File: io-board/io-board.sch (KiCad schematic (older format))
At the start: 12 parts, among them J1 Expansion, J2 Expansion, J3 Conn_01x12, J4 Conn_01x12, J5 Conn_01x06, U1 W65C22NxP, U2 W65C51NxP, U3 74HC138, X1 1.8432MHz

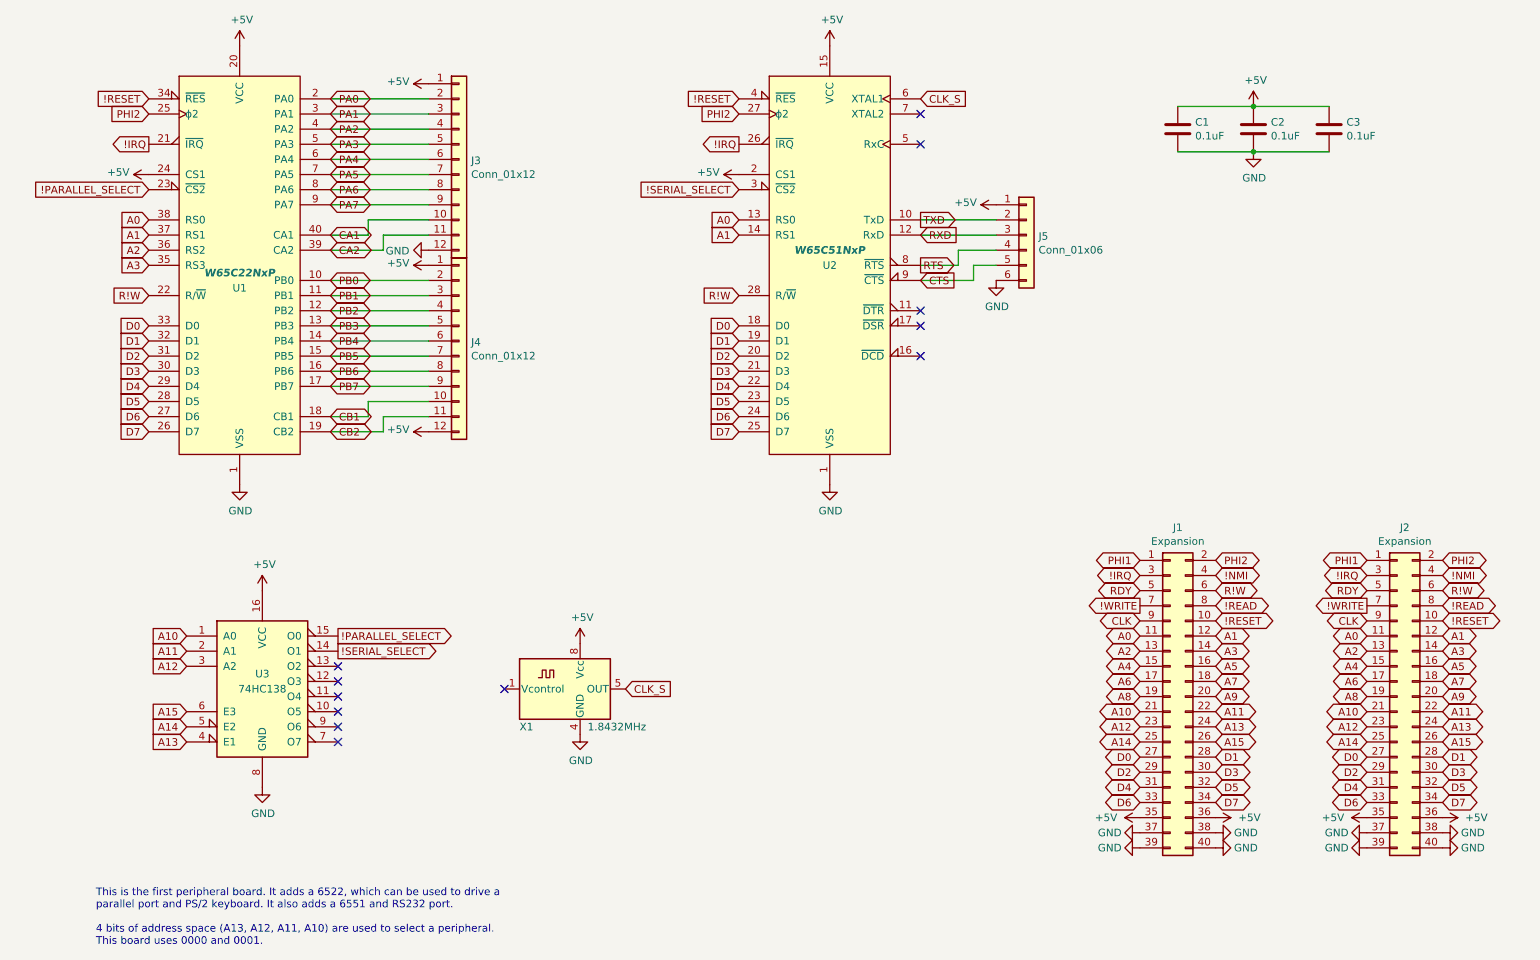
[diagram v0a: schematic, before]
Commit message: remove vga board, finish other boards
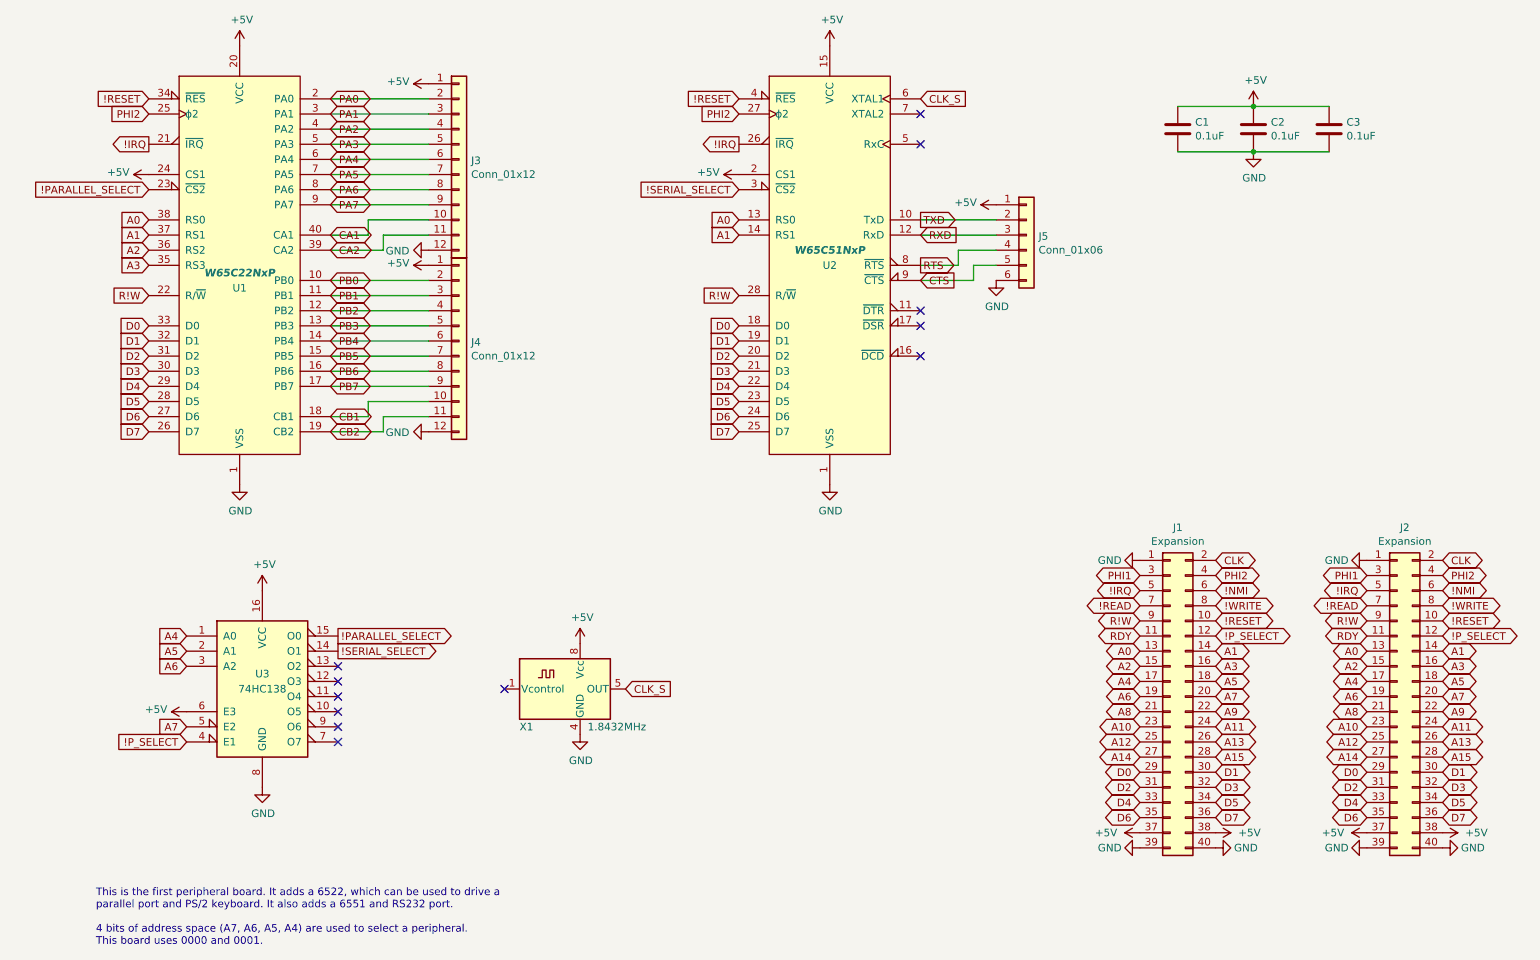
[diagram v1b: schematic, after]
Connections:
- net !IRQ: now also J1.5 (Pin_5), J2.5 (Pin_5); no longer J1.3 (Pin_3), J2.3 (Pin_3)
- net !NMI: now also J1.6 (Pin_6), J2.6 (Pin_6); no longer J1.4 (Pin_4), J2.4 (Pin_4)
- net !READ: now also J1.7 (Pin_7), J2.7 (Pin_7); no longer J1.8 (Pin_8), J2.8 (Pin_8)
- net !WRITE: now also J1.8 (Pin_8), J2.8 (Pin_8); no longer J1.7 (Pin_7), J2.7 (Pin_7)
- net +5V: now also J1.37 (Pin_37), J1.38 (Pin_38), J2.37 (Pin_37), J2.38 (Pin_38), U3.6 (E3); no longer J1.35 (Pin_35), J1.36 (Pin_36), J2.35 (Pin_35), J2.36 (Pin_36), J4.12 (Pin_12)
- net A0: now also J1.13 (Pin_13), J2.13 (Pin_13); no longer J1.11 (Pin_11), J2.11 (Pin_11)
- net A1: now also J1.14 (Pin_14), J2.14 (Pin_14); no longer J1.12 (Pin_12), J2.12 (Pin_12)
- net A10: now also J1.23 (Pin_23), J2.23 (Pin_23); no longer J1.21 (Pin_21), J2.21 (Pin_21), U3.1 (A0)
- net A11: now also J1.24 (Pin_24), J2.24 (Pin_24); no longer J1.22 (Pin_22), J2.22 (Pin_22), U3.2 (A1)
- net A12: now also J1.25 (Pin_25), J2.25 (Pin_25); no longer J1.23 (Pin_23), J2.23 (Pin_23), U3.3 (A2)
- net A13: now also J1.26 (Pin_26), J2.26 (Pin_26); no longer J1.24 (Pin_24), J2.24 (Pin_24), U3.4 (E1)
- net A14: now also J1.27 (Pin_27), J2.27 (Pin_27); no longer J1.25 (Pin_25), J2.25 (Pin_25), U3.5 (E2)
- net A15: now also J1.28 (Pin_28), J2.28 (Pin_28); no longer J1.26 (Pin_26), J2.26 (Pin_26), U3.6 (E3)
- net A2: now also J1.15 (Pin_15), J2.15 (Pin_15); no longer J1.13 (Pin_13), J2.13 (Pin_13)
- net A3: now also J1.16 (Pin_16), J2.16 (Pin_16); no longer J1.14 (Pin_14), J2.14 (Pin_14)
- net A4: now also J1.17 (Pin_17), J2.17 (Pin_17), U3.1 (A0); no longer J1.15 (Pin_15), J2.15 (Pin_15)
- net A5: now also J1.18 (Pin_18), J2.18 (Pin_18), U3.2 (A1); no longer J1.16 (Pin_16), J2.16 (Pin_16)
- net A6: now also J1.19 (Pin_19), J2.19 (Pin_19), U3.3 (A2); no longer J1.17 (Pin_17), J2.17 (Pin_17)
- net A7: now also J1.20 (Pin_20), J2.20 (Pin_20), U3.5 (E2); no longer J1.18 (Pin_18), J2.18 (Pin_18)
- net A8: now also J1.21 (Pin_21), J2.21 (Pin_21); no longer J1.19 (Pin_19), J2.19 (Pin_19)
- net A9: now also J1.22 (Pin_22), J2.22 (Pin_22); no longer J1.20 (Pin_20), J2.20 (Pin_20)
- net CLK: now also J1.2 (Pin_2), J2.2 (Pin_2); no longer J1.9 (Pin_9), J2.9 (Pin_9)
- net D0: now also J1.29 (Pin_29), J2.29 (Pin_29); no longer J1.27 (Pin_27), J2.27 (Pin_27)
- net D1: now also J1.30 (Pin_30), J2.30 (Pin_30); no longer J1.28 (Pin_28), J2.28 (Pin_28)
- net D2: now also J1.31 (Pin_31), J2.31 (Pin_31); no longer J1.29 (Pin_29), J2.29 (Pin_29)
- net D3: now also J1.32 (Pin_32), J2.32 (Pin_32); no longer J1.30 (Pin_30), J2.30 (Pin_30)
- net D4: now also J1.33 (Pin_33), J2.33 (Pin_33); no longer J1.31 (Pin_31), J2.31 (Pin_31)
- net D5: now also J1.34 (Pin_34), J2.34 (Pin_34); no longer J1.32 (Pin_32), J2.32 (Pin_32)
- net D6: now also J1.35 (Pin_35), J2.35 (Pin_35); no longer J1.33 (Pin_33), J2.33 (Pin_33)
- net D7: now also J1.36 (Pin_36), J2.36 (Pin_36); no longer J1.34 (Pin_34), J2.34 (Pin_34)
- net GND: now also J1.1 (Pin_1), J2.1 (Pin_1), J4.12 (Pin_12); no longer J1.37 (Pin_37), J1.38 (Pin_38), J2.37 (Pin_37), J2.38 (Pin_38)
- net PHI1: now also J1.3 (Pin_3), J2.3 (Pin_3); no longer J1.1 (Pin_1), J2.1 (Pin_1)
- net PHI2: now also J1.4 (Pin_4), J2.4 (Pin_4); no longer J1.2 (Pin_2), J2.2 (Pin_2)
- net R!W: now also J1.9 (Pin_9), J2.9 (Pin_9); no longer J1.6 (Pin_6), J2.6 (Pin_6)
- net RDY: now also J1.11 (Pin_11), J2.11 (Pin_11); no longer J1.5 (Pin_5), J2.5 (Pin_5)
- new net !P_SELECT: J1.12 (Pin_12), J2.12 (Pin_12), U3.4 (E1)
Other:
- note added: "This is the first peripheral board. It adds a 6522, which can be used to drive a\nparallel port and PS/2 keyboard. It also adds a 6551 and RS232 port.\n\n4 bits of address space (A7, A6, A5, A4) are used to select a peripheral.\nThis board uses 0000 and 0001."
- note removed: "This is the first peripheral board. It adds a 6522, which can be used to drive a\nparallel port and PS/2 keyboard. It also adds a 6551 and RS232 port.\n\n4 bits of address space (A13, A12, A11, A10) are used to select a peripheral.\nThis board uses 0000 and 0001."

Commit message: Redesign CPU and IO boards
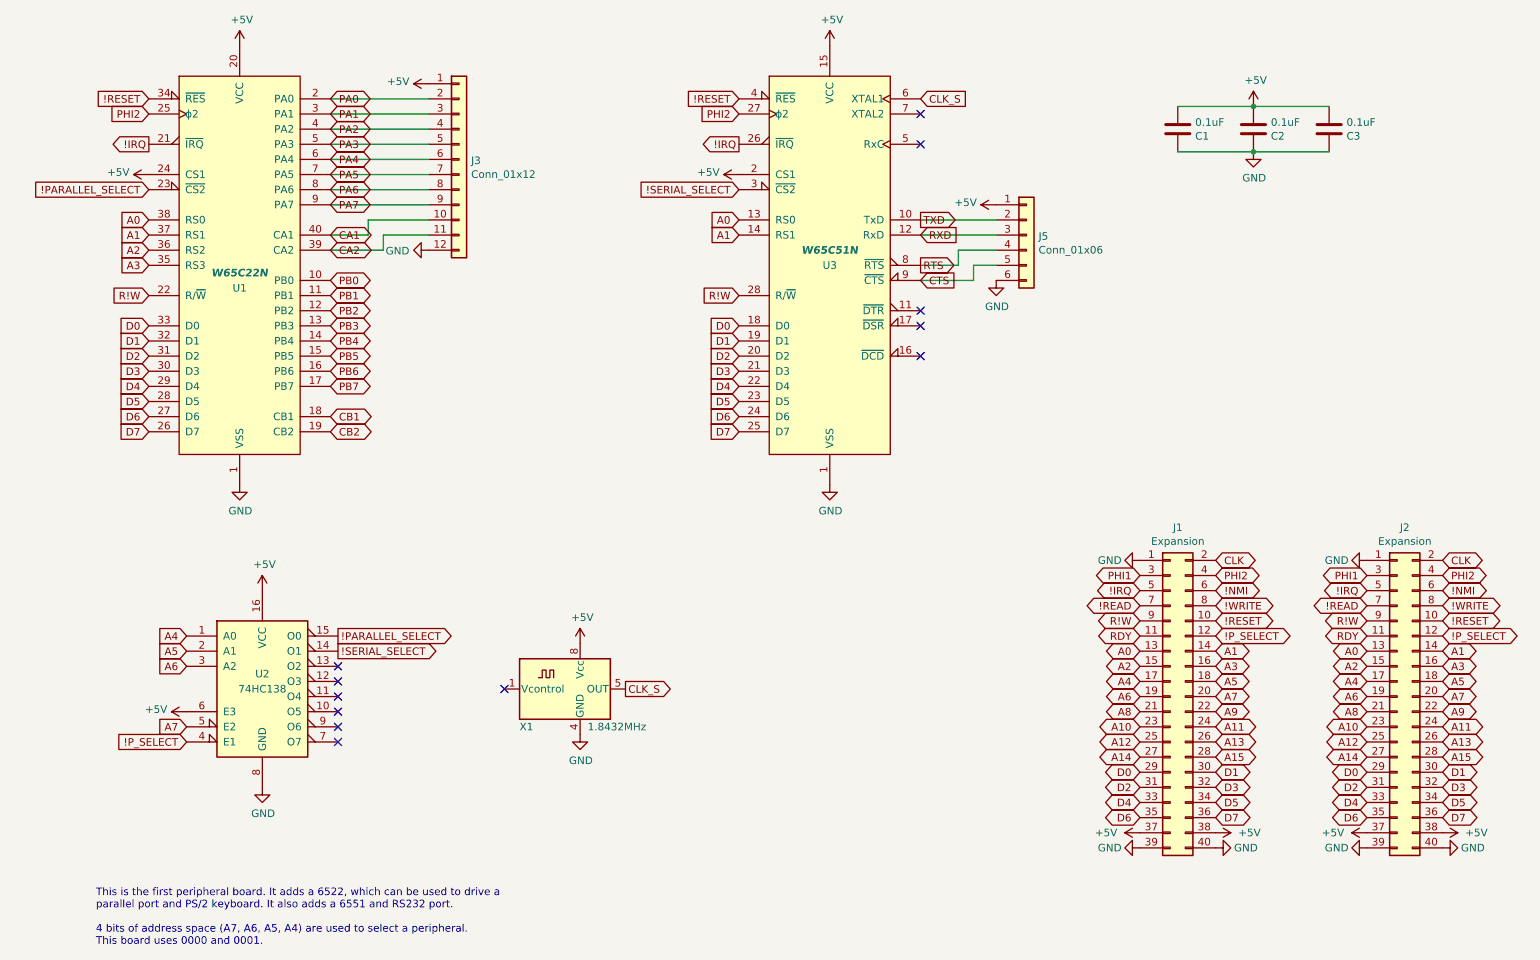
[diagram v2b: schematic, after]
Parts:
- removed J4: Conn_01x12, Connector_PinHeader_2.54mm:PinHeader_1x12_P2.54mm_Horizontal, symbol Connector_Generic:Conn_01x12
- U1: value W65C22NxP -> W65C22N
- U3: renamed from U2; value W65C51NxP -> W65C51N
- renumbered U3 to U2
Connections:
- net +5V: now also C1.2, C2.2, C3.2; no longer C1.1, C2.1, C3.1
- net GND: now also C1.1, C2.1, C3.1; no longer C1.2, C2.2, C3.2
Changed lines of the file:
@@
 $EndComp
 $Comp
-L 65xx:W65C51NxP U2
+L 65xx:W65C51NxP U3
 U 1 1 5FC67B85
 P 5800 2300
-F 0 "U2" H 5800 2300 50  0000 C CNN
-F 1 "W65C51NxP" H 5800 2400 50  0000 C CIB
+F 0 "U3" H 5800 2300 50  0000 C CNN
+F 1 "W65C51N" H 5800 2400 50  0000 C CIB
 F 2 "Package_DIP:DIP-28_W15.24mm_Socket" H 5800 2450 50  0001 C CNN
 F 3 "http://www.westerndesigncenter.com/wdc/documentation/w65c51n.pdf" H 5800 2450 50  0001 C CNN
@@
 NoConn ~ 6400 1500
 $Comp
-L 74xx:74LS138 U3
+L 74xx:74LS138 U2
 U 1 1 5FCA545F
 P 2050 5050
-F 0 "U3" H 2050 5100 50  0000 C CNN
+F 0 "U2" H 2050 5100 50  0000 C CNN
 F 1 "74HC138" H 2050 5000 50  0000 C CNN
 F 2 "Package_DIP:DIP-16_W7.62mm_Socket" H 2050 5050 50  0001 C CNN
@@
 P 1900 2300
 F 0 "U1" H 1900 2150 50  0000 C CNN
-F 1 "W65C22NxP" H 1900 2250 50  0000 C CIB
+F 1 "W65C22N" H 1900 2250 50  0000 C CIB
 F 2 "Package_DIP:DIP-40_W15.24mm_Socket" H 1900 2450 50  0001 C CNN
 F 3 "http://www.westerndesigncenter.com/wdc/documentation/w65c22.pdf" H 1900 2450 50  0001 C CNN
@@
 F 3 "~" H 8100 1400 50  0001 C CNN
 	1    8100 1400
-	1    0    0    -1
+	1    0    0    1
 $EndComp
 $Comp
@@
 F 3 "~" H 8600 1400 50  0001 C CNN
 	1    8600 1400
-	1    0    0    -1
+	1    0    0    1
 $EndComp
 $Comp
@@
 F 3 "~" H 9100 1400 50  0001 C CNN
 	1    9100 1400
-	1    0    0    -1
+	1    0    0    1
 $EndComp
 Wire Wire Line
@@
 $EndComp
 $Comp
-L Connector_Generic:Conn_01x12 J4
-U 1 1 5FCB6E8C
-P 3350 2800
-F 0 "J4" H 3430 2792 50  0000 L CNN
-F 1 "Conn_01x12" H 3430 2701 50  0000 L CNN
-F 2 "Connector_PinHeader_2.54mm:PinHeader_1x12_P2.54mm_Horizontal" H 3430 2655 50  0001 L CNN
-F 3 "~" H 3350 2800 50  0001 C CNN
-	1    3350 2800
-	1    0    0    -1
-$EndComp
-$Comp
-L power:+5V #PWR0105
-U 1 1 5FCBB521
-P 3150 2300
-F 0 "#PWR0105" H 3150 2150 50  0001 C CNN
-F 1 "+5V" V 3165 2428 50  0000 L CNN
-F 2 "" H 3150 2300 50  0001 C CNN
-F 3 "" H 3150 2300 50  0001 C CNN
-	1    3150 2300
-	0    -1   -1   0
-$EndComp
-Wire Wire Line
-	2500 2400 3150 2400
-Wire Wire Line
-	2500 2500 3150 2500
-Wire Wire Line
-	2500 2600 3150 2600
-Wire Wire Line
-	2500 2700 3150 2700
-Wire Wire Line
-	2500 2800 3150 2800
-Wire Wire Line
-	2500 2900 3150 2900
-Wire Wire Line
-	2500 3000 3150 3000
-Wire Wire Line
-	2500 3100 3150 3100
-Wire Wire Line
-	2500 3300 2750 3300
-Wire Wire Line
-	2750 3300 2750 3200
-Wire Wire Line
-	2750 3200 3150 3200
-Wire Wire Line
-	2500 3400 2850 3400
-Wire Wire Line
-	2850 3400 2850 3300
-Wire Wire Line
-	2850 3300 3150 3300
-$Comp
 L Connector_Generic:Conn_01x06 J5
 U 1 1 5FCC838F
@@
 	1    0    0    -1
 $EndComp
-Text GLabel 4450 5100 2    50   Input ~ 0
+Text GLabel 4450 5100 2    50   Output ~ 0
 CLK_S
 $Comp
@@
 Text GLabel 1550 5350 0    50   Input ~ 0
 A7
-$Comp
-L power:GND #PWR0106
-U 1 1 5FCD568B
-P 3150 3400
-F 0 "#PWR0106" H 3150 3150 50  0001 C CNN
-F 1 "GND" V 3155 3272 50  0000 R CNN
-F 2 "" H 3150 3400 50  0001 C CNN
-F 3 "" H 3150 3400 50  0001 C CNN
-	1    3150 3400
-	0    1    1    0
-$EndComp
 $EndSCHEMATC

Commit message: Finish designing and routing new CPU and IO boards
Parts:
- J1, J2: value Expansion -> EXP
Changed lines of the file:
@@
 P 8050 5150
 F 0 "J1" H 8100 6267 50  0000 C CNN
-F 1 "Expansion" H 8100 6176 50  0000 C CNN
+F 1 "EXP" H 8100 6176 50  0000 C CNN
 F 2 "Connector_PinHeader_2.54mm:PinHeader_2x20_P2.54mm_Vertical" H 8050 5150 50  0001 C CNN
 F 3 "~" H 8050 5150 50  0001 C CNN
@@
 P 9550 5150
 F 0 "J2" H 9600 6267 50  0000 C CNN
-F 1 "Expansion" H 9600 6176 50  0000 C CNN
+F 1 "EXP" H 9600 6176 50  0000 C CNN
 F 2 "Connector_PinHeader_2.54mm:PinHeader_2x20_P2.54mm_Vertical" H 9550 5150 50  0001 C CNN
 F 3 "~" H 9550 5150 50  0001 C CNN
